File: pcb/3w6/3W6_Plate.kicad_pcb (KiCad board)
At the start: 2 copper layers, 243.2 x 106 mm, 47 parts

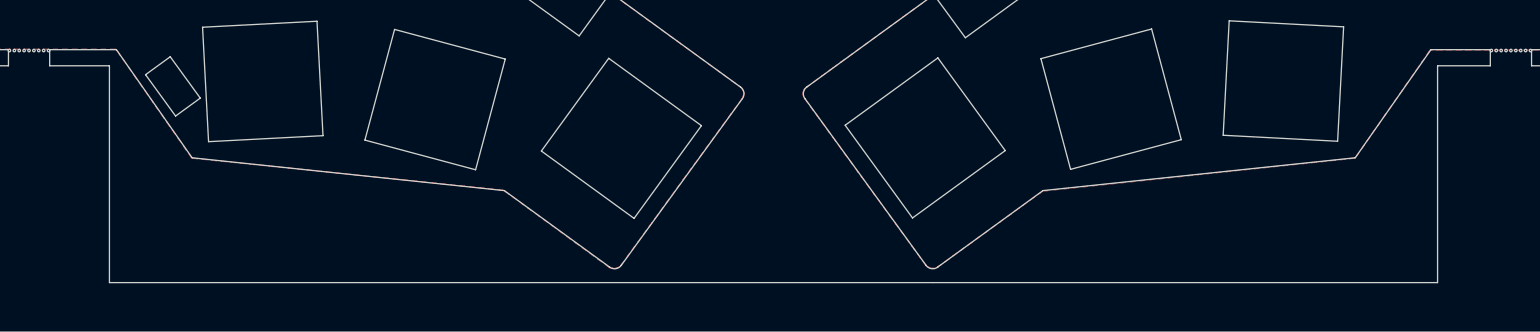
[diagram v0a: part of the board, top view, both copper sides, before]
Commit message: chg: plate to match pcb after trackball support
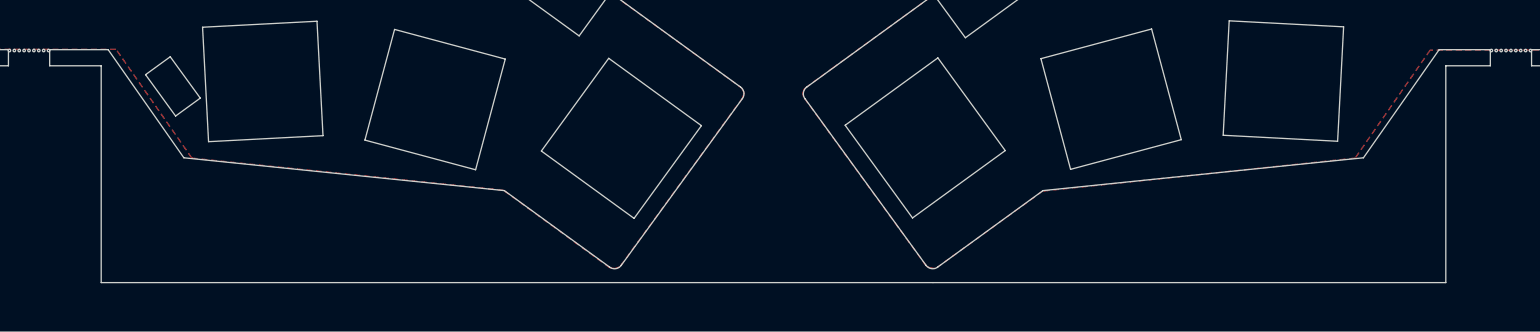
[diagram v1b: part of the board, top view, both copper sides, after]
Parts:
- moved G*** 1.00 mm to (260.2, 85.9)
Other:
- outline, holes or cut-outs redrawn
